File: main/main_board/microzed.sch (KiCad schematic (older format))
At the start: 7 parts, among them M1 microzed, U6 AP3761C-25SP, X1 microzed

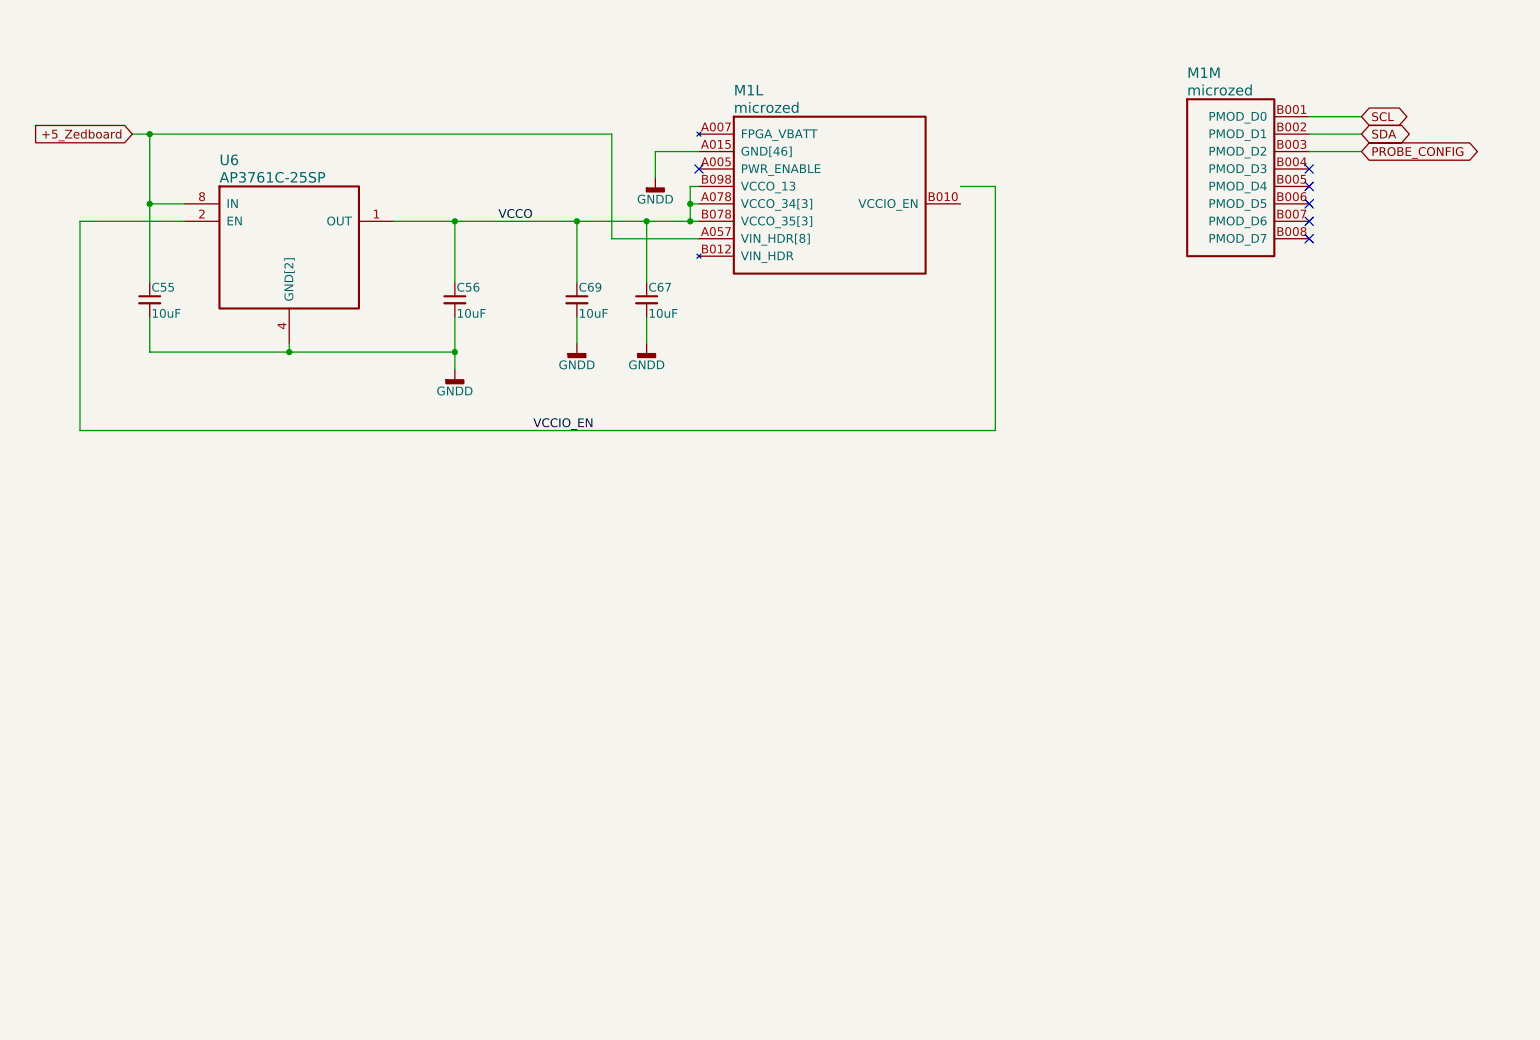
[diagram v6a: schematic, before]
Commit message: Various preparations for routing the main board. Cleaned up the BOM and reconciled it with the Digikey BOM, so lots of component attributes have changed. This involved pinning down some components which had been vague, especially ferrite beads and chip capacitors. 1uF capacitors have all been changed to 10uF. Changed CARDSEL lines to be buffered rather than filtered, since we had the unused buffers sitting there. Another pass on the Microzed pin mapping.  Brought out the DEBUG LVDS line, and tweaked orderings. Added RC filter and pullups on I2C and PROBE_CONFIG.  We might need level translators here to get >=3.3V Added mount holes for the low volt regulator daughtercard, and dimensioned the connector location.
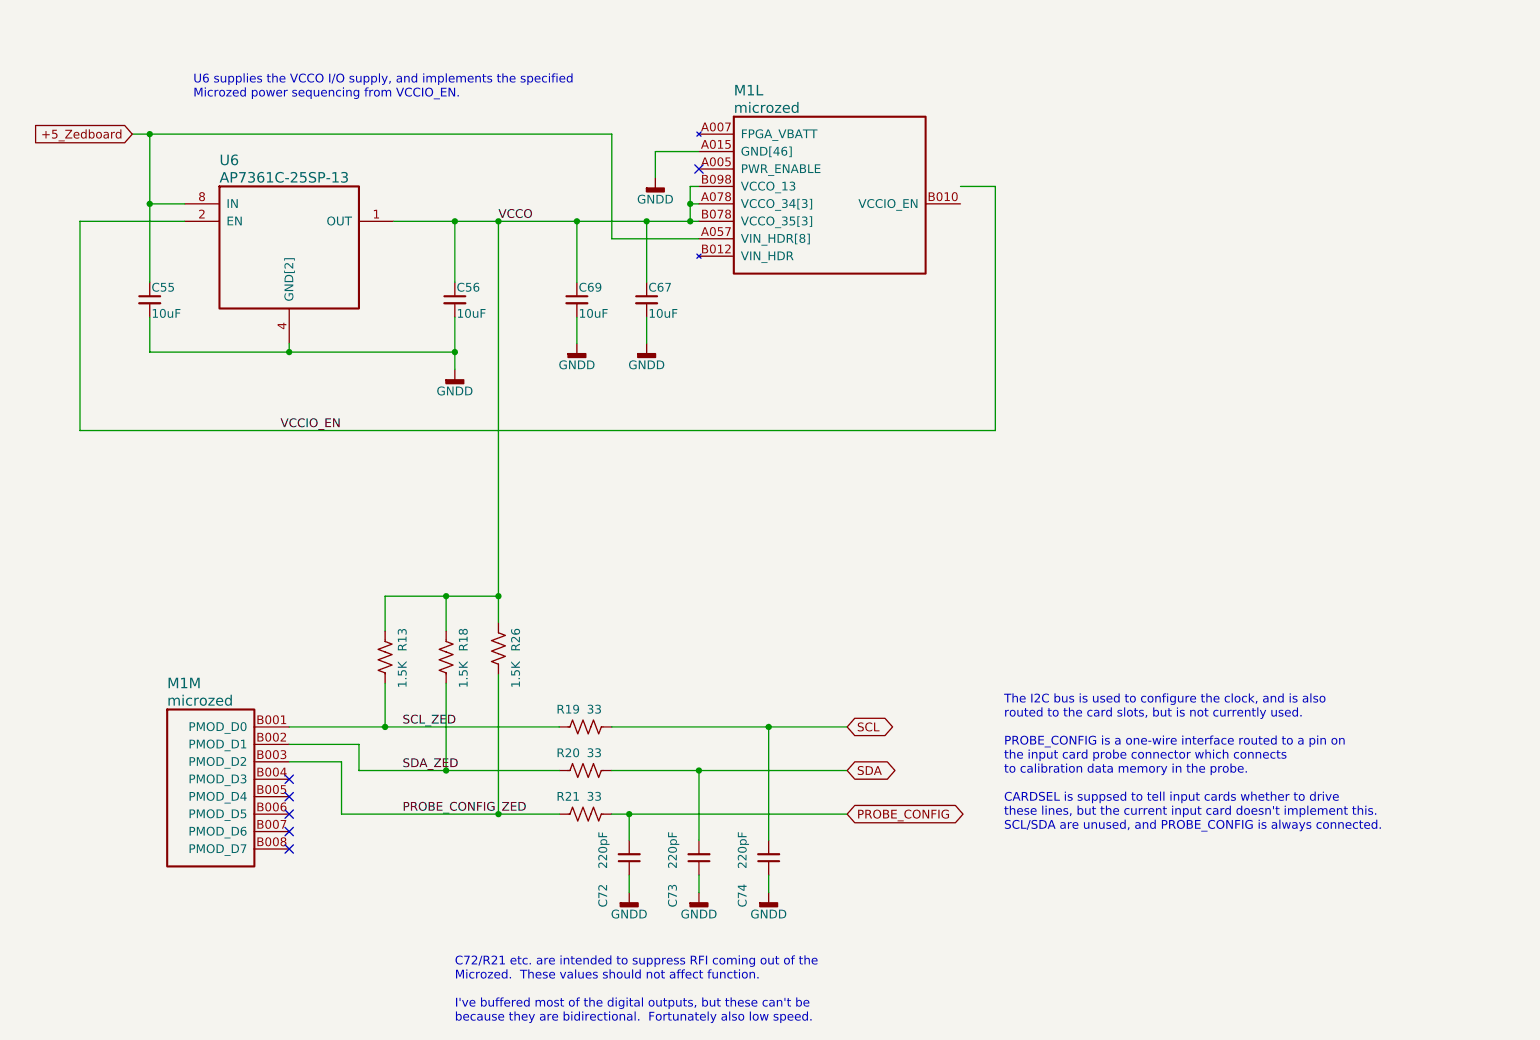
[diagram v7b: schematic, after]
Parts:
- added C72, C73, C74: 220pF, Capacitor_SMD:C_0603_1608Metric, symbol Device:C_Small
- added R13, R18, R26: 1.5K, Resistor_SMD:R_0603_1608Metric, symbol Device:R_US
- added R19, R20, R21: 33, Resistor_SMD:R_0603_1608Metric, symbol Device:R_US
- C55, C56, C67, C69: DK line 29 -> 20; Manufacturer (none) -> AVX
- U6: value AP3761C-25SP -> AP7361C-25SP-13; DK line (none) -> 24; Description (none) -> IC REG LINEAR 2.5V 1A 8SO; Digikey (none) -> AP7361C-33SP-13DICT-ND; MPN (none) -> AP7361C-25SP-13; Manufacturer (none) -> Diodes Incorporated
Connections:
- net labels added: PROBE_CONFIG_ZED, SCL_ZED, SDA_ZED
- wire segments 37 -> 66
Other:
- note added: "C72/R21 etc. are intended to suppress RFI coming out of the\nMicrozed. These values should not affect function.\n\nI've buffered most of the digital outputs, but these can't be \nbecause they are bidirectional. Fortunately also low speed."
- note added: "The I2C bus is used to configure the clock, and is also\nrouted to the card slots, but is not currently used.\n\nPROBE_CONFIG is a one-wire interface routed to a pin on\nthe input card probe connector which connects\nto calibration data memory in the probe.\n\nCARDSEL is suppsed to tell input cards whether to drive\nthese lines, but the current input card doesn't implement this.\nSCL/SDA are unus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"
- note added: "U6 supplies the VCCO I/O supply, and implements the specified \nMicrozed power sequencing from VCCIO_EN.\n"
- moved on the sheet: M1M

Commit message: Main board is now fully routed and passing DRC. Minor changes related to pin remapping. I2C and one-wire pullups are to OVDD 3.3V, not VCCIO 2.5V. Changes to supply decoupling and VREF- net in reference.sch, suggested by routing.
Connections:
- net VCCIO_EN: now also X1.B010 (VCCIO_EN)
- net VCCO: no longer R13.2, R18.2, R26.2
- new net OVDD: R13.2, R18.2, R26.2
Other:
- note added: "+3.3V"
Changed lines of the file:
@@
 	2200 2250 2200 2700
 Wire Wire Line
-	6850 2150 7050 2150
+	6850 2250 7050 2250
 Wire Wire Line
 	1800 2350 2400 2350
@@
 Wire Wire Line
 	4850 2450 5350 2450
-Wire Wire Line
-	7050 2150 7050 3550
 NoConn ~ 3000 5550
 NoConn ~ 3000 5650
@@
 	3550 4500 3550 4700
 Wire Wire Line
-	3950 2350 4200 2350
-Connection ~ 4200 2350
-Wire Wire Line
-	4200 2350 4650 2350
-Wire Wire Line
 	3900 4700 3900 4500
 Wire Wire Line
@@
 $EndComp
 Wire Wire Line
-	4200 2350 4200 4500
-Wire Wire Line
 	4200 5750 4550 5750
 Wire Wire Line
@@
 	3900 4500 4200 4500
 Connection ~ 3900 4500
-Connection ~ 4200 4500
 Wire Wire Line
 	4200 4500 4200 4650
+Wire Wire Line
+	3950 2350 4650 2350
+$Comp
+L ilemt_input:OVDD #PWR0133
+U 1 1 5F0D8254
+P 3550 4350
+AR Path="/5E525F87/5F0D8254" Ref="#PWR0133"  Part="1"
+AR Path="/5E525FFE/5F0D8254" Ref="#PWR?"  Part="1"
+AR Path="/5E525FC9/5F0D8254" Ref="#PWR?"  Part="1"
+F 0 "#PWR0133" H 3550 4200 50  0001 C CNN
+F 1 "OVDD" H 3550 4500 50  0000 C CNN
+F 2 "" H 3550 4350 50  0001 C CNN
+F 3 "" H 3550 4350 50  0001 C CNN
+	1    3550 4350
+	1    0    0    -1
+$EndComp
+Wire Wire Line
+	3550 4350 3550 4500
+Connection ~ 3550 4500
+Text Notes 3700 4450 0    50   ~ 0
++3.3V
+Wire Wire Line
+	7050 2250 7050 3550
 $EndSCHEMATC
